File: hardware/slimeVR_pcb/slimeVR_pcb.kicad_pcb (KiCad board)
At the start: 2 copper layers, 40 x 43 mm, 62 parts, among them J1 HRO_TYPE-C-31-M-12, Q1 8205A, SW1 SK12D07VG4, SW2 SW_Push, U1 ESP32-S2-WROVER, U10 AP2112K-3.3, U2 TP4057, U3 ICM-45686, U5 QMC6309, U6 TPS25200DRVR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

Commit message: add silkscreen labels
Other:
- board text added: "@H3wastooshort /slimeinator"
- board text added: "Project: LilyFox, H3, Elios Schematic & Layout: H3"
- board text added: "Slimeinator v0"
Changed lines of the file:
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@@
 		(tags "ESP32-S2  ESP32  WIFI")
 		(property "Reference" "U1"
-			(at 10.64 -18.905 180)
+			(at -10.36 -13.905 180)
 			(layer "F.SilkS")
 			(effects
@@
 		(layer "Edge.Cuts")
 	)
+	(gr_text "@H3wastooshort\n/slimeinator"
+		(at 169 38.5 0)
+		(layer "F.SilkS")
+		(effects
+			(font
+				(size 1 1)
+				(thickness 0.1)
+			)
+			(justify left bottom)
+		)
+	)
 	(gr_text "-"
 		(at 177.25 72.9 0)
@@
 		)
 	)
+	(gr_text "Slimeinator v0"
+		(at 164 38 0)
+		(layer "B.SilkS")
+		(effects
+			(font
+				(size 2 2)
+				(thickness 0.15)
+			)
+			(justify mirror)
+		)
+	)
+	(gr_text "Project: LilyFox, H3, Elios\nSchematic & Layout: H3"
+		(at 164 40 0)
+		(layer "B.SilkS")
+		(effects
+			(font
+				(size 1 1)
+				(thickness 0.1)
+			)
+			(justify top mirror)
+		)
+	)

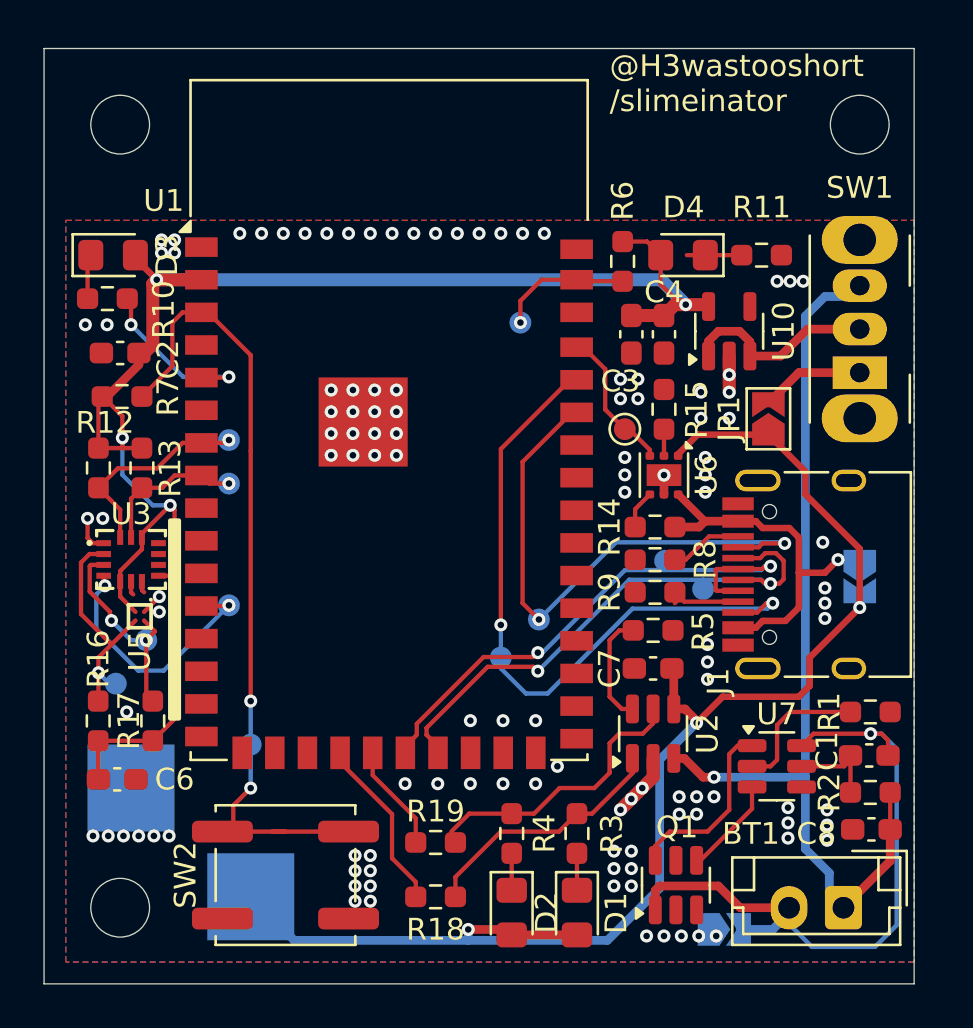
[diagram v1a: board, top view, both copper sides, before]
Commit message: add. design rules, pcb cleanup
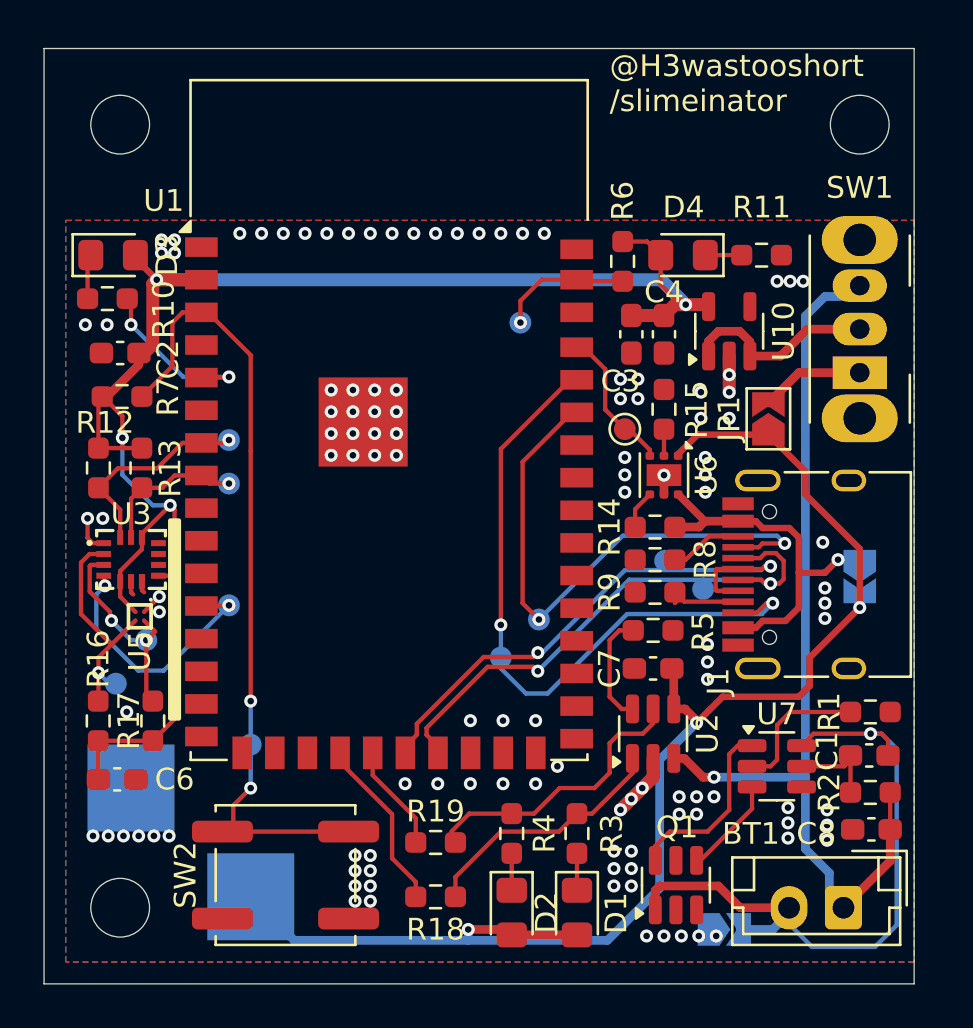
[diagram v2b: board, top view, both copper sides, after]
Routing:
- net /BOOT: track 37.2 -> 36.6 mm

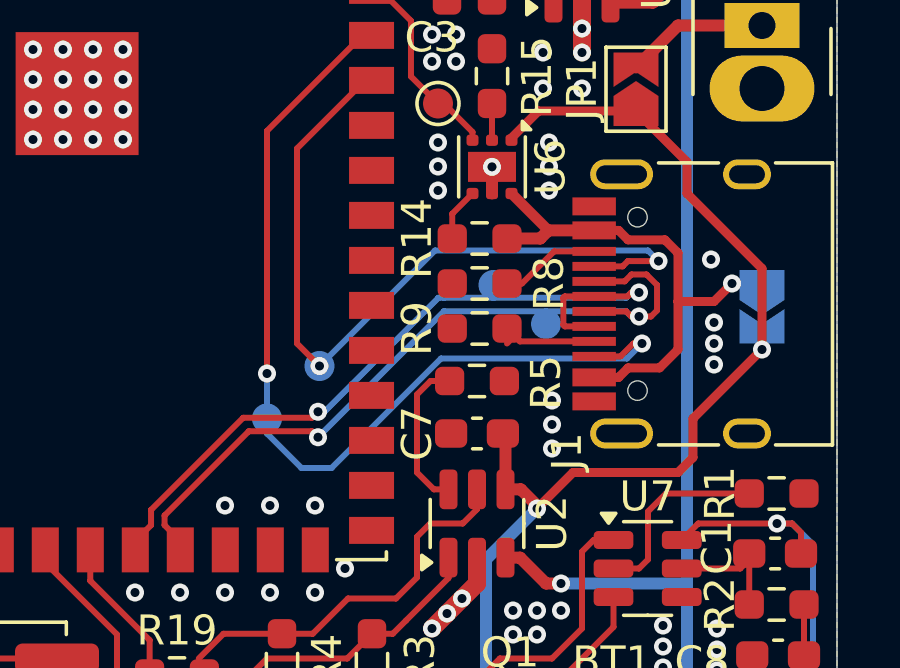
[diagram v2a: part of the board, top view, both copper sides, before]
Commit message: allow ESP to read/write CC pins for future use
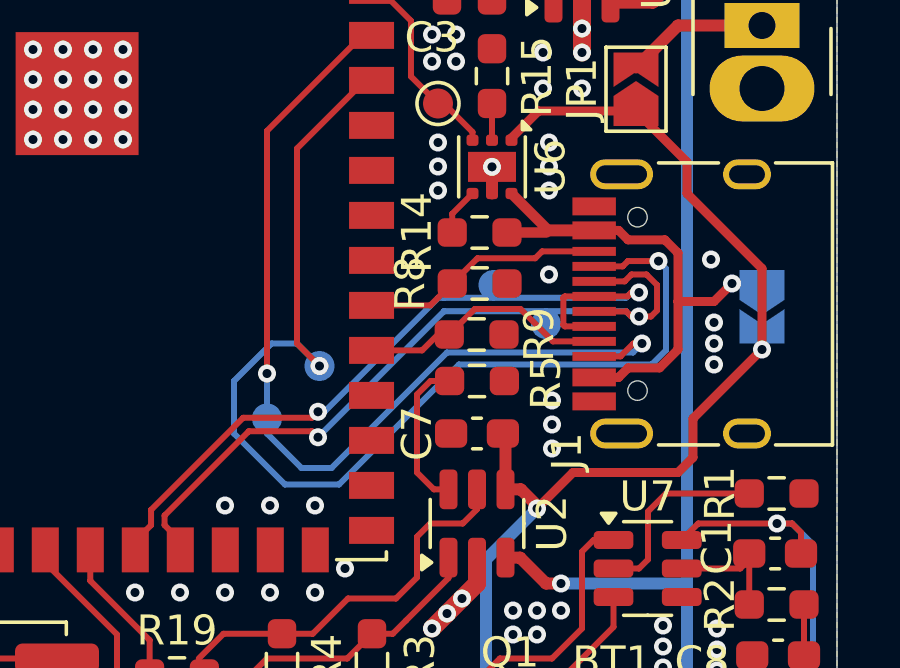
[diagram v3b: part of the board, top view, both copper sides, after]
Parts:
- D1: value red -> yellow
- D2: value blue -> white
- D3: value green -> yellow
- moved R9 0.22 mm to (171.0, 60.7), turned to 0 degrees
- moved R14 0.20 mm to (171.1, 57.3)
- turned R8 to 0 degrees
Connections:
- J1 pad A5: Net-(J1-CC1) -> /CC1
- J1 pad B5: Net-(J1-CC2) -> /CC2
- R8 pad 1: Net-(J1-CC2) -> /CC2
- R9 pad 1: Net-(J1-CC1) -> /CC1
- U1 pad 31: unconnected-(U1-IO37-Pad31) -> /CC1
- U1 pad 32: unconnected-(U1-IO38-Pad32) -> /CC2
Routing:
- net /TX: track 26.2 -> 38.7 mm
- net /CC1: track 0.00 -> 8.44 mm
- net /CC2: track 0.00 -> 8.17 mm
- net Net-(J1-CC2): track 3.35 -> 0.00 mm
- net Net-(J1-CC1): track 3.18 -> 0.00 mm
- net GND: track 9.62 -> 9.72 mm, vias 116 -> 117

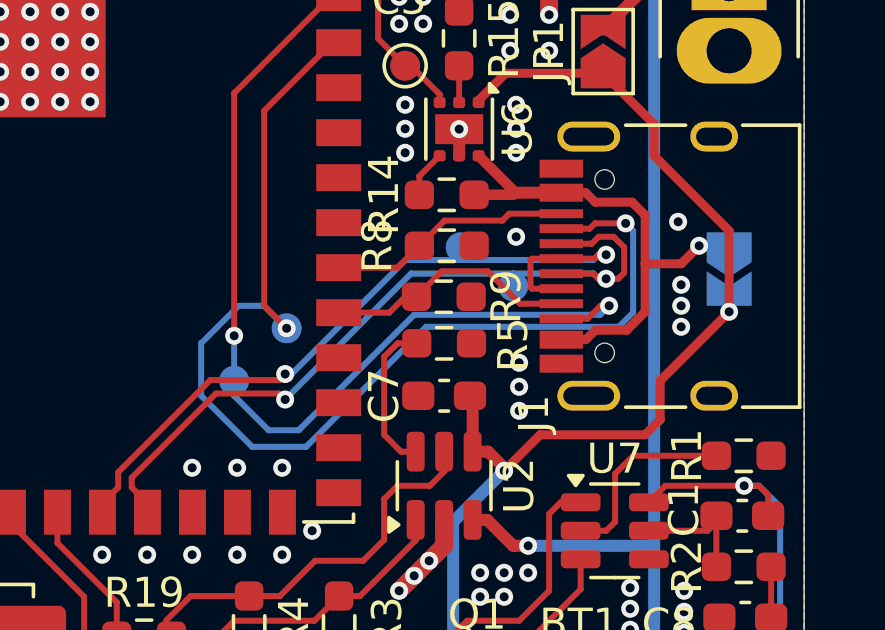
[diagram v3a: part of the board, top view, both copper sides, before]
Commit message: tried to use an FUSB302 to supply vconn
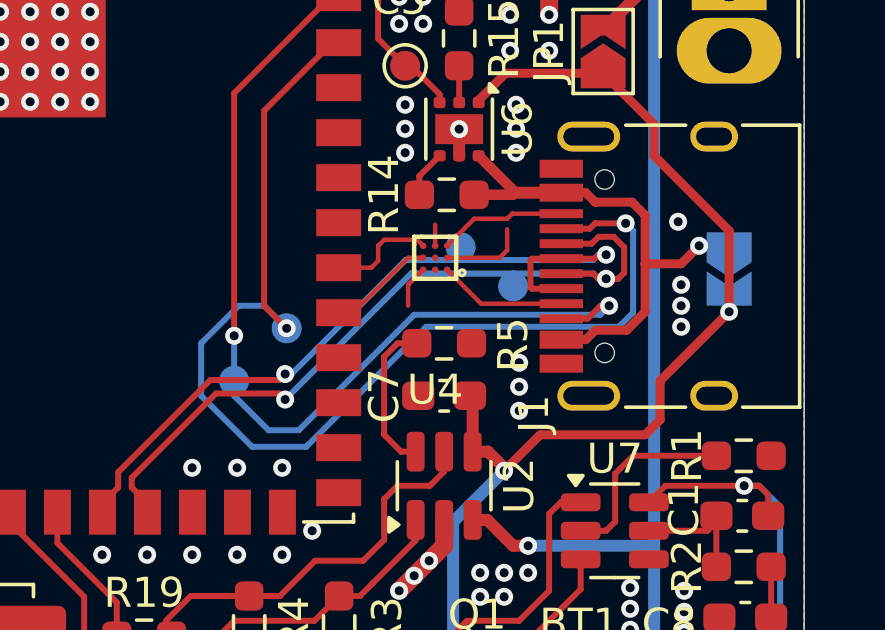
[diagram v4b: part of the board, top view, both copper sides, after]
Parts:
- removed R8, R9: 5k1, Resistor_SMD:R_0603_1608Metric_Pad0.98x0.95mm_HandSolder
- added U4: FUSB302BUCX, easyeda2kicad:WLCSP-9_L1.3-W1.2-R3-C3-P0.40-TL, F.Cu at (170.7, 59.4)
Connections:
- U1 pad 31: /CC1 -> Net-(U1-IO37)
- U1 pad 32: /CC2 -> Net-(U1-IO38)
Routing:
- net +3V3: track 78.3 -> 82.5 mm
- net /CC1: track 8.44 -> 4.26 mm
- net /CC2: track 8.17 -> 4.23 mm
- net Net-(U1-IO37): track 0.00 -> 3.57 mm
- net Net-(U1-IO38): track 0.00 -> 3.56 mm
- net GND: track 9.72 -> 10.3 mm, vias 117 -> 116

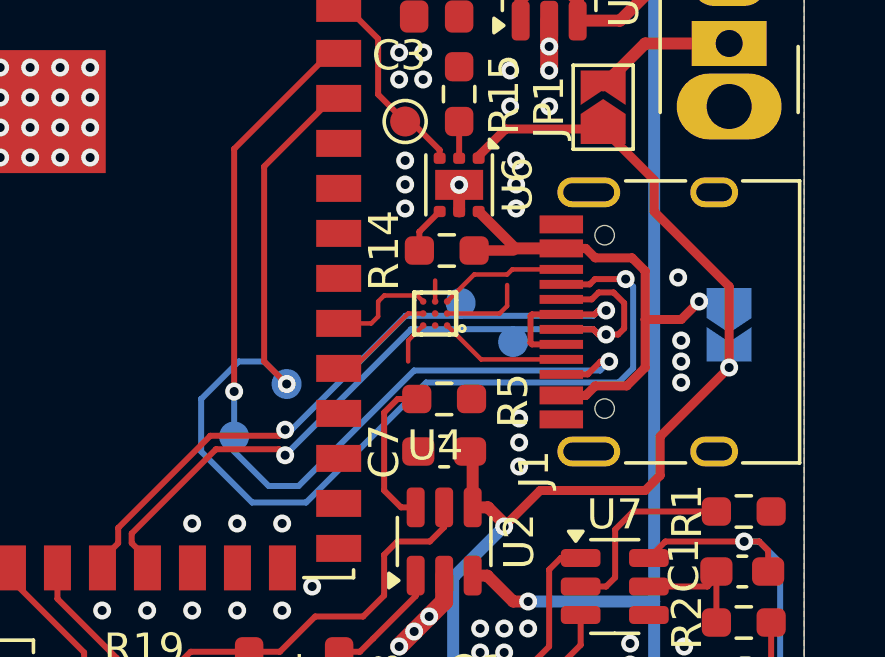
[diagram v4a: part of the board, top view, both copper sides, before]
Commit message: give up on FUSB302 idea i need to supply power via USB C safely, without adding more comonents i need 2 datalines for i2c i could detect shorting of sbu 1 and sbu 2, then use the CC or D+/D- pins for i2c comms
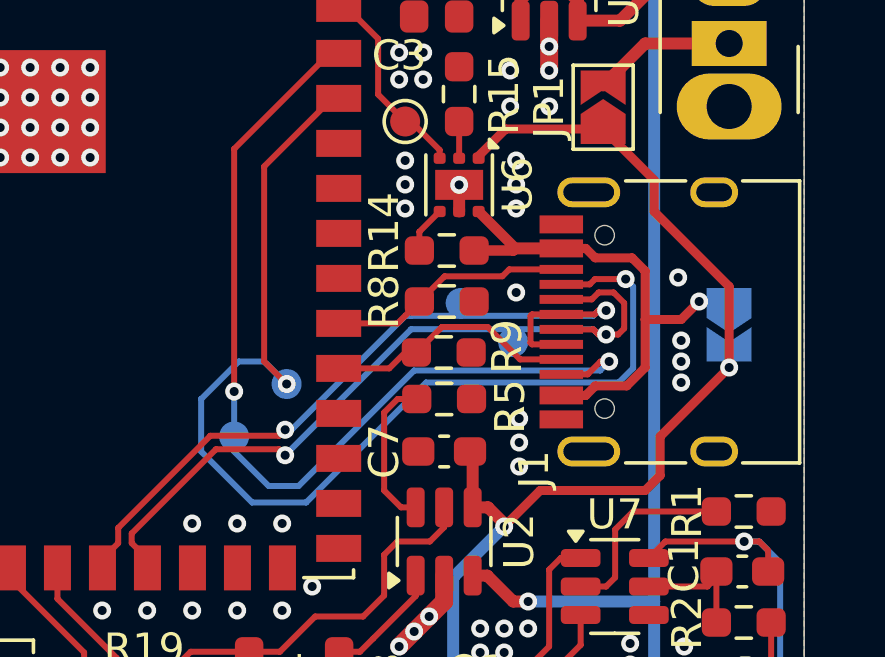
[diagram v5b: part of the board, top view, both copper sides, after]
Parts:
- removed U4: FUSB302BUCX, easyeda2kicad:WLCSP-9_L1.3-W1.2-R3-C3-P0.40-TL
- added R8: 5k1, Resistor_SMD:R_0603_1608Metric_Pad0.98x0.95mm_HandSolder, F.Cu at (171.1, 59.0)
- added R9: 5k1, Resistor_SMD:R_0603_1608Metric_Pad0.98x0.95mm_HandSolder, F.Cu at (171.0, 60.7)
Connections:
- U1 pad 31: Net-(U1-IO37) -> /CC1
- U1 pad 32: Net-(U1-IO38) -> /CC2
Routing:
- net +3V3: track 82.5 -> 78.3 mm
- net /CC1: track 4.26 -> 8.44 mm
- net /CC2: track 4.23 -> 8.17 mm
- net Net-(U1-IO37): track 3.57 -> 0.00 mm
- net Net-(U1-IO38): track 3.56 -> 0.00 mm
- net GND: track 10.3 -> 9.72 mm, vias 116 -> 117

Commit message: actually fix typo...
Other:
- board text added: "Project: LilyFox, H3, Eleos Schematic & Layout: H3"
- board text removed: "Project: LilyFox, H3, Elios Schematic & Layout: H3"
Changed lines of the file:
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@@
 		)
 	)
-	(gr_text "Project: LilyFox, H3, Elios\nSchematic & Layout: H3"
+	(gr_text "Project: LilyFox, H3, Eleos\nSchematic & Layout: H3"
 		(at 164 40 0)
 		(layer "B.SilkS")

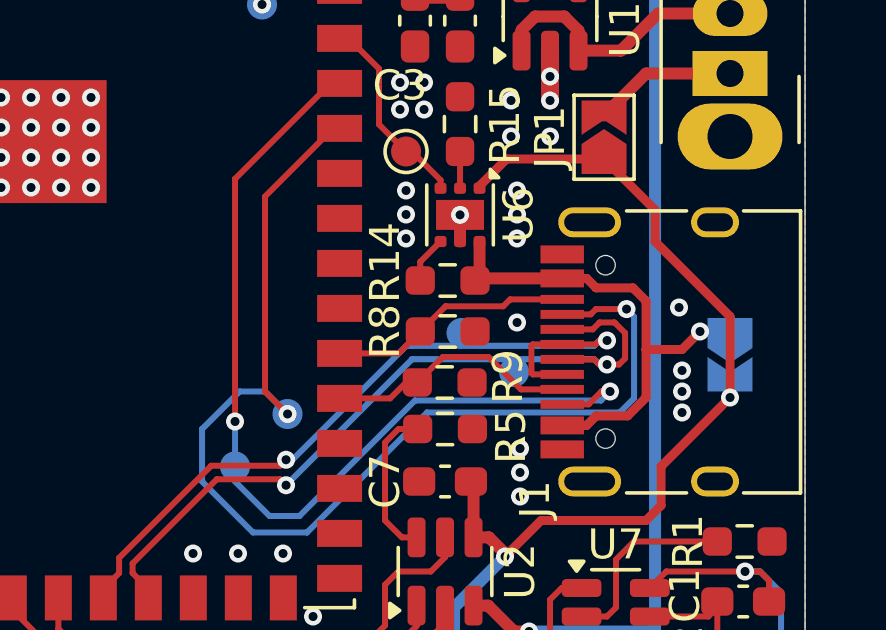
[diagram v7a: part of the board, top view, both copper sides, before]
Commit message: fixup partsel, fixup silkscreen
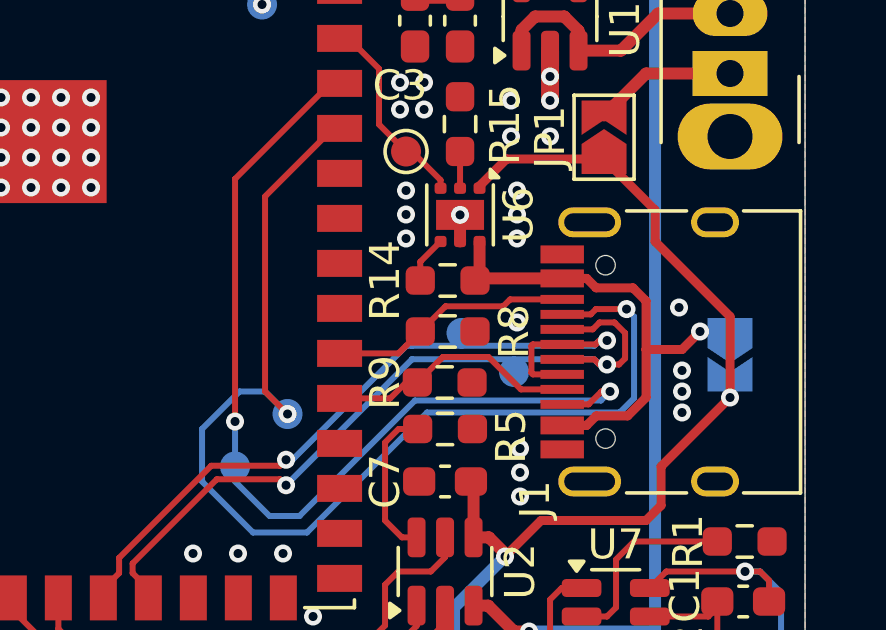
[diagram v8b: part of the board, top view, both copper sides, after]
